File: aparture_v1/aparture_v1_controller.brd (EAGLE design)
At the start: 79.8 x 59.1 mm, 34 parts, among them IC1 LD117AS33TR, IC3 LTC1966CMS8

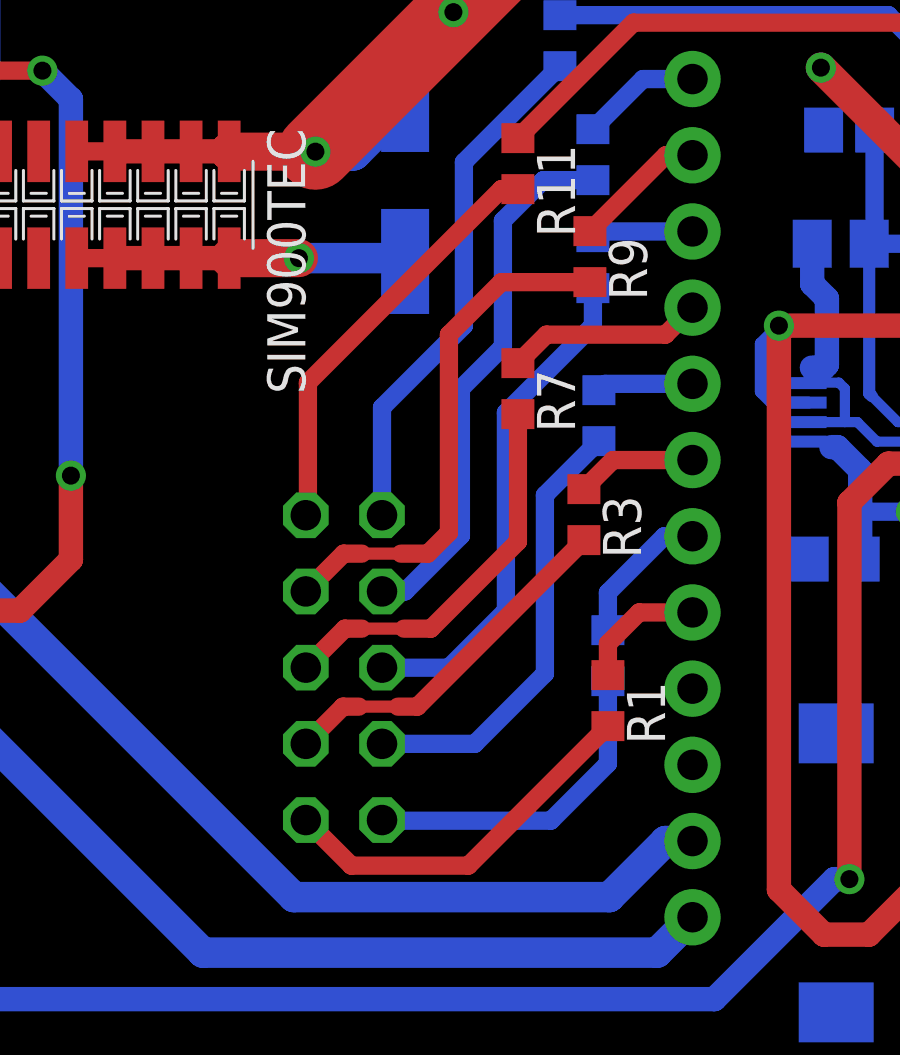
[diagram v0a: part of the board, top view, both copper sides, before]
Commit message: resize boards
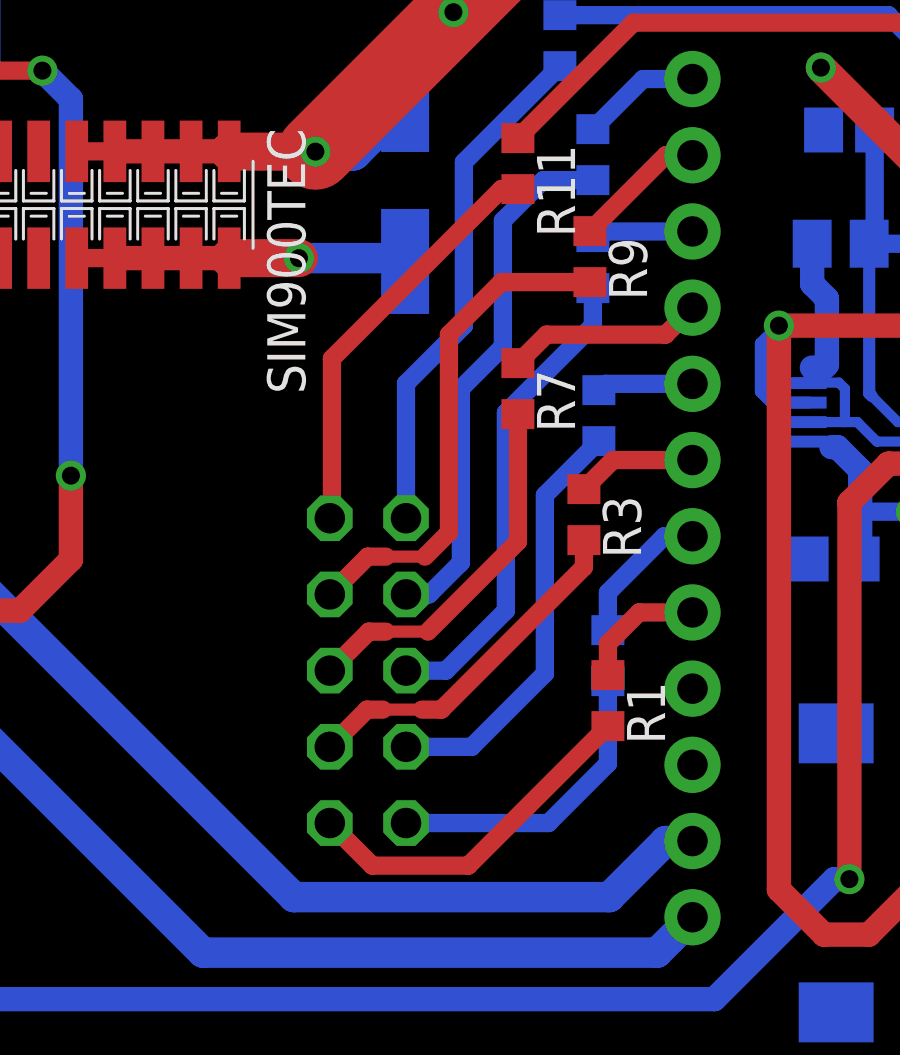
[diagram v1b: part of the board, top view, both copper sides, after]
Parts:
- moved JP3 0.81 mm to (50.5, 14.0)
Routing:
- net N$1: track 12.6 -> 11.8 mm
- net N$6: track 11.1 -> 10.3 mm
- net N$9: track 14.9 -> 14.1 mm
- net N$10: track 16.9 -> 16.1 mm
- net N$4: track 17.6 -> 16.8 mm
- net N$3: track 13.1 -> 12.3 mm
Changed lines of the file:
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@@
 <element name="R4" library="resistor" package="M0805" value="R100K" x="71.32" y="28.18" rot="MR180"/>
 <element name="R5" library="resistor" package="M0805" value="R100K" x="66.26" y="28.23" rot="MR180"/>
-<element name="JP3" library="pinhead" package="2X05" value="" x="49.7" y="14.1" rot="MR90"/>
+<element name="JP3" library="pinhead" package="2X05" value="" x="50.5" y="14" rot="MR90"/>
 <element name="R1" library="rcl" package="R0603" value="" x="58.5" y="13" rot="R270"/>
 <element name="R2" library="rcl" package="R0603" value="" x="58.5" y="14.5" rot="MR90"/>
@@
 <contactref element="R1" pad="2"/>
 <contactref element="JP3" pad="1"/>
-<wire x1="48.43" y1="9.02" x2="49.95" y2="7.5" width="0.6096" layer="1"/>
-<wire x1="49.95" y1="7.5" x2="53.85" y2="7.5" width="0.6096" layer="1"/>
 <wire x1="53.85" y1="7.5" x2="58.5" y2="12.15" width="0.6096" layer="1"/>
+<wire x1="53.85" y1="7.5" x2="50.65" y2="7.5" width="0.6096" layer="1"/>
+<wire x1="50.65" y1="7.5" x2="49.23" y2="8.92" width="0.6096" layer="1"/>
 </signal>
 <signal name="N$2">
 <contactref element="R3" pad="2"/>
 <contactref element="JP3" pad="3"/>
-<wire x1="48.43" y1="11.56" x2="49.67" y2="12.8" width="0.6096" layer="1"/>
-<wire x1="49.67" y1="12.8" x2="50.2" y2="12.8" width="0.6096" layer="1"/>
-<wire x1="50.2" y1="12.8" x2="51.5" y2="12.8" width="0.4064" layer="1"/>
-<wire x1="51.5" y1="12.8" x2="52.15" y2="12.8" width="0.6096" layer="1"/>
-<wire x1="52.15" y1="12.8" x2="57.7" y2="18.35" width="0.6096" layer="1"/>
+<wire x1="50.47" y1="12.7" x2="51" y2="12.7" width="0.6096" layer="1"/>
+<wire x1="51" y1="12.7" x2="52.3" y2="12.7" width="0.4064" layer="1"/>
+<wire x1="52.3" y1="12.7" x2="52.95" y2="12.7" width="0.6096" layer="1"/>
+<wire x1="50.47" y1="12.7" x2="49.23" y2="11.46" width="0.6096" layer="1"/>
+<wire x1="52.95" y1="12.7" x2="57.7" y2="17.45" width="0.6096" layer="1"/>
+<wire x1="57.7" y1="17.45" x2="57.7" y2="18.35" width="0.6096" layer="1"/>
 </signal>
 <signal name="N$3">
@@
 <contactref element="JP3" pad="5"/>
 <wire x1="55.5" y1="22.55" x2="55.5" y2="18.3" width="0.6096" layer="1"/>
-<wire x1="55.5" y1="18.3" x2="52.6" y2="15.4" width="0.6096" layer="1"/>
-<wire x1="52.6" y1="15.4" x2="51.7" y2="15.4" width="0.6096" layer="1"/>
-<wire x1="51.7" y1="15.4" x2="50.3" y2="15.4" width="0.4064" layer="1"/>
-<wire x1="50.3" y1="15.4" x2="49.73" y2="15.4" width="0.6096" layer="1"/>
-<wire x1="49.73" y1="15.4" x2="48.43" y2="14.1" width="0.6096" layer="1"/>
+<wire x1="55.5" y1="18.3" x2="52.5" y2="15.3" width="0.6096" layer="1"/>
+<wire x1="52.5" y1="15.3" x2="51.1" y2="15.3" width="0.4064" layer="1"/>
+<wire x1="51.1" y1="15.3" x2="50.53" y2="15.3" width="0.6096" layer="1"/>
+<wire x1="50.53" y1="15.3" x2="49.23" y2="14" width="0.6096" layer="1"/>
 </signal>
 <signal name="N$4">
 <contactref element="R9" pad="2"/>
 <contactref element="JP3" pad="7"/>
-<wire x1="48.43" y1="16.64" x2="49.69" y2="17.9" width="0.6096" layer="1"/>
-<wire x1="49.69" y1="17.9" x2="50.3" y2="17.9" width="0.6096" layer="1"/>
-<wire x1="50.3" y1="17.9" x2="51.6" y2="17.9" width="0.4064" layer="1"/>
-<wire x1="51.6" y1="17.9" x2="52.5" y2="17.9" width="0.6096" layer="1"/>
-<wire x1="52.5" y1="17.9" x2="53.2" y2="18.6" width="0.6096" layer="1"/>
+<wire x1="49.23" y1="16.54" x2="50.49" y2="17.8" width="0.6096" layer="1"/>
+<wire x1="50.49" y1="17.8" x2="51.1" y2="17.8" width="0.6096" layer="1"/>
+<wire x1="51.1" y1="17.8" x2="52.4" y2="17.8" width="0.4064" layer="1"/>
 <wire x1="53.2" y1="18.6" x2="53.2" y2="25.2" width="0.6096" layer="1"/>
 <wire x1="53.2" y1="25.2" x2="54.95" y2="26.95" width="0.6096" layer="1"/>
 <wire x1="54.95" y1="26.95" x2="57.9" y2="26.95" width="0.6096" layer="1"/>
+<wire x1="53.2" y1="18.6" x2="52.4" y2="17.8" width="0.6096" layer="1"/>
 </signal>
 <signal name="N$5">
@@
 <contactref element="JP3" pad="9"/>
 <wire x1="55.5" y1="30.05" x2="54.95" y2="30.05" width="0.6096" layer="1"/>
-<wire x1="54.95" y1="30.05" x2="48.5" y2="23.6" width="0.6096" layer="1"/>
-<wire x1="48.5" y1="23.6" x2="48.5" y2="19.25" width="0.6096" layer="1"/>
-<wire x1="48.5" y1="19.25" x2="48.43" y2="19.18" width="0.6096" layer="1"/>
+<wire x1="49.3" y1="19.15" x2="49.23" y2="19.08" width="0.6096" layer="1"/>
+<wire x1="49.3" y1="19.15" x2="49.3" y2="24.4" width="0.6096" layer="1"/>
+<wire x1="49.3" y1="24.4" x2="54.95" y2="30.05" width="0.6096" layer="1"/>
 </signal>
 <signal name="N$6">
 <contactref element="R2" pad="1"/>
 <contactref element="JP3" pad="2"/>
-<wire x1="58.5" y1="10.9" x2="56.6" y2="9" width="0.6096" layer="16"/>
-<wire x1="56.6" y1="9" x2="50.99" y2="9" width="0.6096" layer="16"/>
-<wire x1="50.99" y1="9" x2="50.97" y2="9.02" width="0.6096" layer="16"/>
 <wire x1="58.5" y1="13.65" x2="58.5" y2="10.9" width="0.6096" layer="16"/>
+<wire x1="58.5" y1="10.9" x2="56.52" y2="8.92" width="0.6096" layer="16"/>
+<wire x1="56.52" y1="8.92" x2="51.77" y2="8.92" width="0.6096" layer="16"/>
 </signal>
 <signal name="N$9">
 <contactref element="R6" pad="1"/>
 <contactref element="JP3" pad="4"/>
-<wire x1="54.06" y1="11.56" x2="50.97" y2="11.56" width="0.6096" layer="16"/>
 <wire x1="58.2" y1="21.65" x2="56.4" y2="19.85" width="0.6096" layer="16"/>
 <wire x1="56.4" y1="19.85" x2="56.4" y2="13.9" width="0.6096" layer="16"/>
-<wire x1="56.4" y1="13.9" x2="54.06" y2="11.56" width="0.6096" layer="16"/>
+<wire x1="56.4" y1="13.9" x2="53.96" y2="11.46" width="0.6096" layer="16"/>
+<wire x1="53.96" y1="11.46" x2="51.77" y2="11.46" width="0.6096" layer="16"/>
 </signal>
 <signal name="N$10">
 <contactref element="R8" pad="1"/>
 <contactref element="JP3" pad="6"/>
-<wire x1="53.2" y1="14.1" x2="50.97" y2="14.1" width="0.6096" layer="16"/>
 <wire x1="58" y1="26.75" x2="58" y2="25.5" width="0.6096" layer="16"/>
 <wire x1="58" y1="25.5" x2="55.1" y2="22.6" width="0.6096" layer="16"/>
 <wire x1="55.1" y1="22.6" x2="55.1" y2="16" width="0.6096" layer="16"/>
-<wire x1="55.1" y1="16" x2="53.2" y2="14.1" width="0.6096" layer="16"/>
+<wire x1="55.1" y1="16" x2="53.1" y2="14" width="0.6096" layer="16"/>
+<wire x1="53.1" y1="14" x2="51.77" y2="14" width="0.6096" layer="16"/>
 </signal>
 <signal name="N$11">
@@
 <wire x1="55" y1="29" x2="55" y2="24.8" width="0.6096" layer="16"/>
 <wire x1="55" y1="24.8" x2="53.6" y2="23.4" width="0.6096" layer="16"/>
-<wire x1="53.6" y1="23.4" x2="53.6" y2="18.5" width="0.6096" layer="16"/>
-<wire x1="53.6" y1="18.5" x2="51.74" y2="16.64" width="0.6096" layer="16"/>
-<wire x1="51.74" y1="16.64" x2="50.97" y2="16.64" width="0.6096" layer="16"/>
+<wire x1="53.6" y1="23.4" x2="53.6" y2="17.6" width="0.6096" layer="16"/>
+<wire x1="52.54" y1="16.54" x2="51.77" y2="16.54" width="0.6096" layer="16"/>
+<wire x1="53.6" y1="17.6" x2="52.54" y2="16.54" width="0.6096" layer="16"/>
 </signal>
 <signal name="N$12">
@@
 <wire x1="56.9" y1="34.15" x2="53.7" y2="30.95" width="0.6096" layer="16"/>
 <wire x1="53.7" y1="30.95" x2="53.7" y2="25.5" width="0.6096" layer="16"/>
-<wire x1="53.7" y1="25.5" x2="50.97" y2="22.77" width="0.6096" layer="16"/>
-<wire x1="50.97" y1="22.77" x2="50.97" y2="19.18" width="0.6096" layer="16"/>
+<wire x1="53.7" y1="25.5" x2="51.77" y2="23.57" width="0.6096" layer="16"/>
+<wire x1="51.77" y1="23.57" x2="51.77" y2="19.08" width="0.6096" layer="16"/>
 </signal>
 </signals>
